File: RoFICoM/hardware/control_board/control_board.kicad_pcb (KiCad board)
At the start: 2 copper layers, 46 x 46 mm, 44 parts, among them J1 Skirt Cable, J2 M+, J3 M-, Q1 DMP6050SFG, Q2 SSM3K72KCT, Q3 DMP6050SFG, Q4 DMP6050SFG, Q5 SSM3K72KCT, Q6 DMP6050SFG, U1 STM32G071GBU6, U2 DRV8837C, U3 BU52272NUZ, U4 MIC5365, U5 BU52272NUZ, U6 ACS70331, U7 ACS70331

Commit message: RoFICoM: Route ContorlBoard v0.2
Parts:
- added C8: 470n, Capacitor_SMD:C_0402_1005Metric, F.Cu at (128.2, 74.3)
- added J4: SWD, Connector_PinHeader_2.54mm:PinHeader_1x05_P2.54mm_Vertical, F.Cu at (134.8, 79.4)
- added J5: DBG_UART, Connector_PinSocket_2.54mm:PinSocket_1x03_P2.54mm_Vertical, F.Cu at (134.8, 76.8)
- added J6: SYS_CON, rofi:pogo_row_4_3, F.Cu at (140.0, 107.0)
- added J7: SLIDER, Connector_PinHeader_1.27mm:PinHeader_1x01_P1.27mm_Vertical, F.Cu at (147.8, 79.1)
- moved R7 63.0 mm to (121.5, 100.3), turned to 270 degrees
- moved R11 62.5 mm to (121.5, 95.3), turned to 270 degrees
- moved U7 62.0 mm to (125.7, 100.3), turned to 180 degrees
- moved R10 60.3 mm to (122.0, 98.4), turned to 180 degrees
- moved R8 60.1 mm to (122.5, 100.3), turned to 90 degrees
- moved Q5 59.0 mm to (122.3, 97.3), turned to 90 degrees
- moved R9 57.1 mm to (121.5, 93.1), turned to 90 degrees
- moved D3 56.2 mm to (122.7, 93.1)
- moved Q4 55.9 mm to (125.7, 93.1), turned to 270 degrees
- moved C7 55.8 mm to (126.7, 102.6), turned to 180 degrees
- moved Q6 53.8 mm to (125.7, 96.6), turned to 270 degrees
- moved D1 38.8 mm to (153.1, 83.5)
- moved Q1 38.0 mm to (125.8, 80.5), turned to 270 degrees
- moved D2 35.9 mm to (122.9, 80.5), turned to 90 degrees
- moved R4 35.1 mm to (121.7, 80.5), turned to 90 degrees
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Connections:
- C2 pad 1: +3V3 -> GND
- C2 pad 2: GND -> +3V3
- U1 pad 1: IN_U -> INT_U
- U1 pad 11: INT_U -> LIMIT_2
- U1 pad 13: INT_I -> LIMIT_1
- U1 pad 14: EXT_U -> POT_SENSE
- U1 pad 17: SENSE_B -> SENSE_A
- U1 pad 2: Net-(U1-Pad2) -> INT_SW
- U1 pad 20: EXT_SW -> SENSE_B
- U1 pad 23: LIMIT_1 -> EXT_I
- U1 pad 24: LIMIT_2 -> EXT_U
- U1 pad 25: EXT_I -> EXT_SW
- U1 pad 28: SENSE_A -> INT_I
- U1 pad 6: INT_SW -> IN_U
- U2 pad 5: MOTOR -> MOTOR_PWM
- U2 pad 6: MOTOR_PWM -> MOTOR
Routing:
- net +3V3: track 1.19 -> 142.2 mm, vias 0 -> 11
- net INT_SW: track 0.00 -> 65.8 mm, vias 0 -> 2
- net INT_U: track 1.06 -> 60.0 mm, vias 0 -> 2
- net INT_I: track 0.00 -> 57.7 mm, vias 0 -> 2
- net SPI_MISO: track 0.00 -> 52.7 mm, vias 0 -> 1
- net EXT_SW: track 0.00 -> 47.3 mm, vias 0 -> 4
- net IN_U: track 0.00 -> 47.2 mm, vias 0 -> 2
- net SPI_SS: track 0.00 -> 45.0 mm, vias 0 -> 1
- net DBG_RX: track 0.00 -> 44.3 mm, vias 0 -> 2
- net EXT_U: track 0.00 -> 41.7 mm, vias 0 -> 4
- net DBG_TX: track 0.00 -> 41.4 mm, vias 0 -> 2
- net EXT_I: track 0.00 -> 37.9 mm, vias 0 -> 2
- net GND: track 12.3 -> 49.6 mm, vias 3 -> 14
- net SPI_SCK: track 0.00 -> 37.3 mm, vias 0 -> 1
- net LIMIT_1: track 0.00 -> 34.3 mm
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- added copper zone on B.Cu, net GND
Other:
- board size 46 x 46 mm -> 48.5 x 48.5 mm
- net class Default: via_dia 0.8 -> 0.6
- board text added: "CL SS IO"
- board text added: "Control Board v0.2 3/2019 ro.fi.muni.cz"
- board text added: "DBG"
- board text added: "GND 3V3 RST IO CLK"
- board text added: "GND RX TX"
- board text added: "RoFICoM"
- board text added: "SWD"
- board text added: "VCC GND INT EXT"

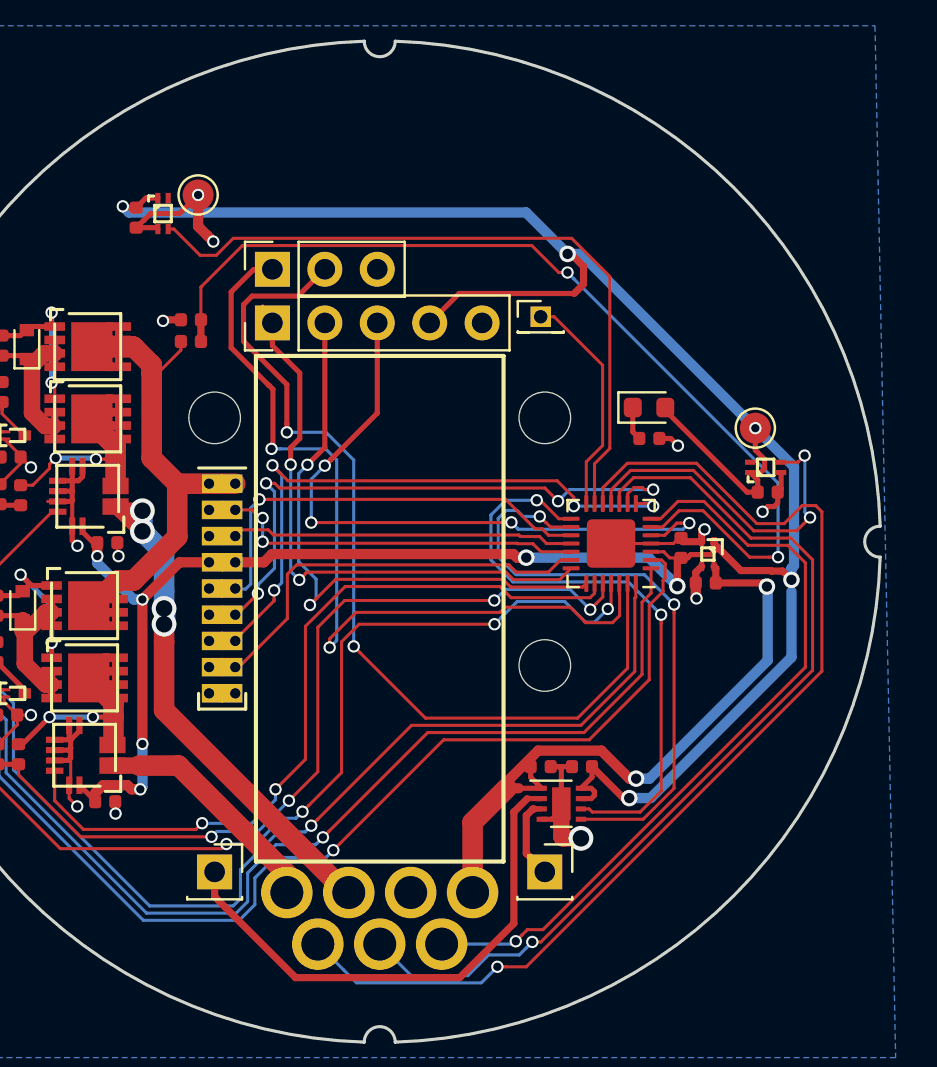
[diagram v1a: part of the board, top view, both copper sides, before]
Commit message: RoFICoM: Change footprint of the MCU
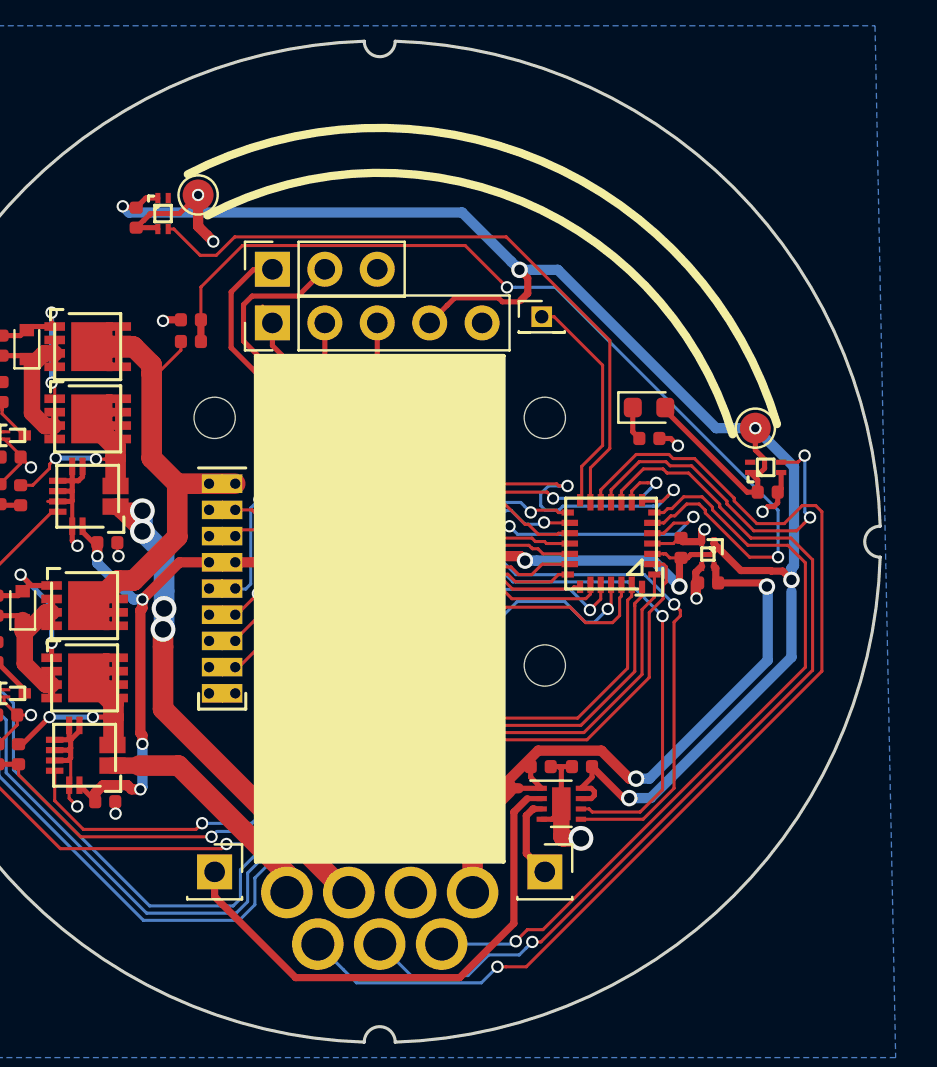
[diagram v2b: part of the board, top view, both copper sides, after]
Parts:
- U1: footprint Package_DFN_QFN:UQFN-28-1EP_4x4mm_P0.4mm_EP2.35x2.35mm -> rofi:UFQFPN28
- moved C1 0.11 mm to (155.9, 92.0)
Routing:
- net TX: track 31.3 -> 36.3 mm
- net +3V3: track 142.2 -> 138.9 mm
- net GND: track 49.6 -> 47.7 mm
- net LIMIT_1: track 34.3 -> 32.6 mm
- net RST: track 31.7 -> 32.4 mm
- net EXT_U: track 41.7 -> 41.1 mm
- net IN_U: track 47.2 -> 46.6 mm
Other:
- board text added: "Control Board v0.3 4/2019 ro.fi.muni.cz"
- board text removed: "Control Board v0.2 3/2019 ro.fi.muni.cz"

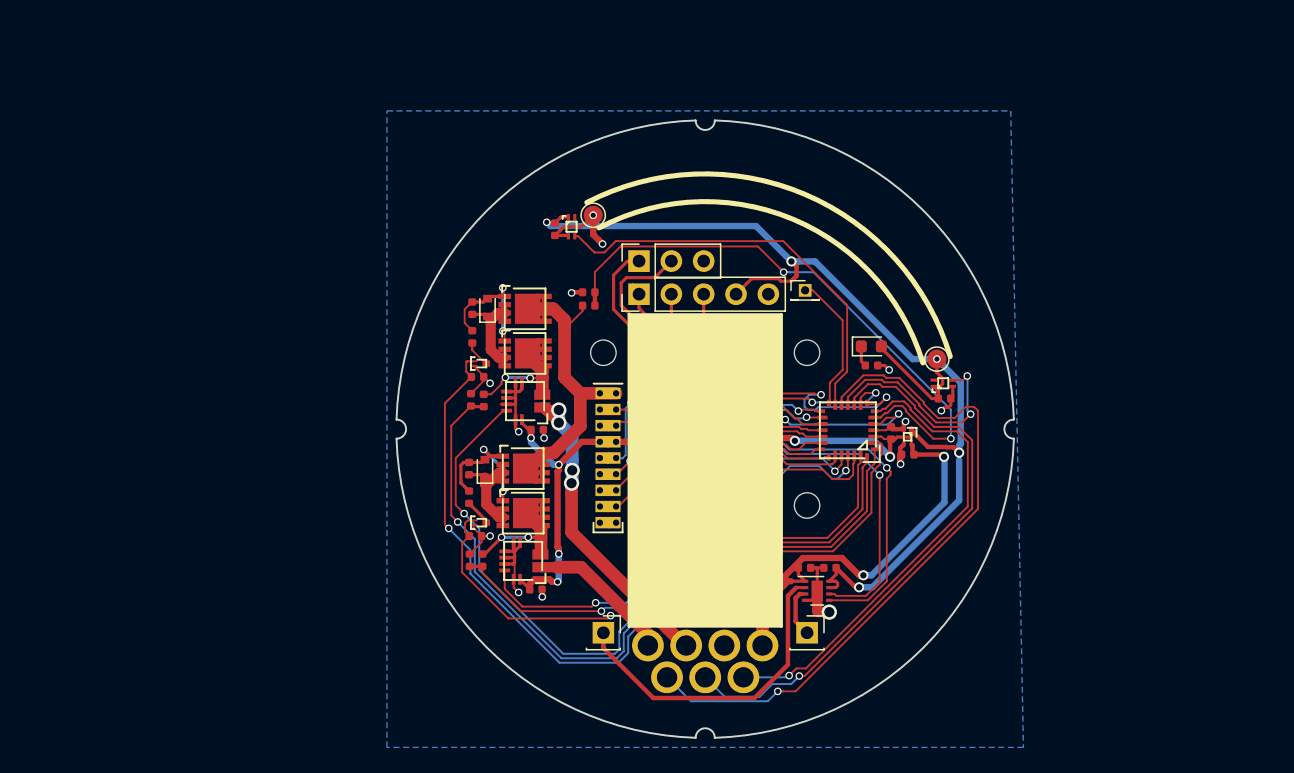
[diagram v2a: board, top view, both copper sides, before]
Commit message: RoFICoM: Add new board revision
- change voltage regulator and switching transistors
- fix wrong wiring of SWD
- add Molex board-to-board connectors for system and debugging
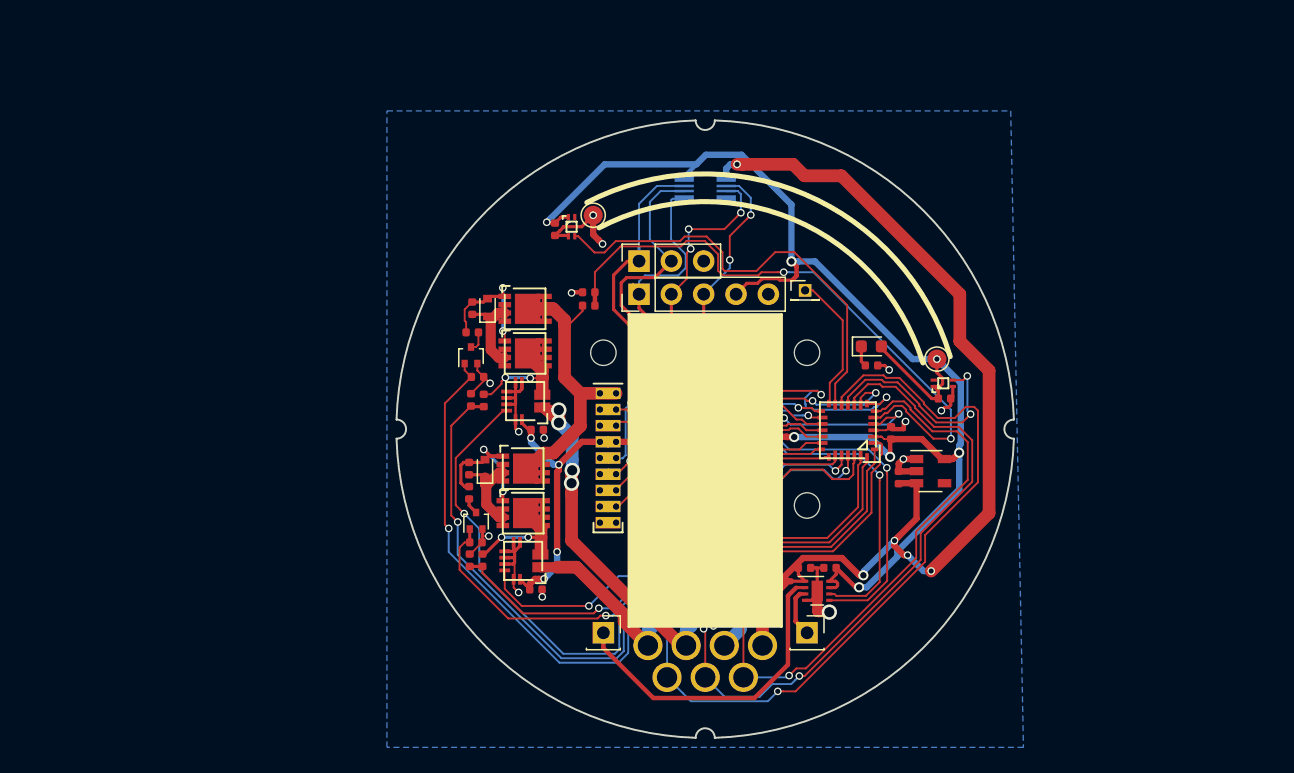
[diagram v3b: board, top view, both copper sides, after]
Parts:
- added J8: DBG, rofi:molex-505006-0812, B.Cu at (140.0, 71.1)
- added J9: SYS_CON_2, rofi:molex-505006-0812, B.Cu at (140.0, 102.5)
- Q2, Q5: value SSM3K72KCT -> SSM3K72CFS; footprint rofi:CST3 -> Package_TO_SOT_SMD:SOT-416
- U4: value MIC5365 -> NCP718ASN330T1G; footprint rofi:MLF-4 -> Package_TO_SOT_SMD:SOT-23-5
- moved U4 3.24 mm to (157.7, 93.3), turned to 0 degrees
- moved C1 1.94 mm to (155.2, 93.8), turned to 90 degrees
- moved Q2 0.96 mm to (121.6, 84.2)
- moved R10 0.50 mm to (122.0, 98.9)
- moved R11 0.35 mm to (121.5, 95.0)
- moved R6 0.35 mm to (121.7, 82.4), turned to 0 degrees
- moved Q5 0.34 mm to (122.0, 97.2)
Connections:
- U1 pad 20: SENSE_B -> SWDIO
- U1 pad 22: SWDIO -> SENSE_B
- U3 pad 4: Net-(U3-Pad4) -> (no net)
- U4 pad 1: +3V3 -> GND
- U4 pad 3: GND -> VCC
- U4 pad 4: VCC -> (no net)
- U5 pad 4: Net-(U5-Pad4) -> (no net)
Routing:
- net VCC: track 32.2 -> 84.9 mm, vias 2 -> 6
- net SPI_SCK: track 37.3 -> 50.6 mm, vias 1 -> 2
- net SWCLK: track 28.9 -> 41.2 mm
- net RST: track 32.4 -> 43.8 mm, vias 4 -> 6
- net SWDIO: track 28.6 -> 39.1 mm, vias 2 -> 5
- net DBG_TX: track 41.4 -> 51.7 mm
- net DBG_RX: track 44.4 -> 54.1 mm
- net SPI_MISO: track 53.2 -> 62.4 mm, vias 1 -> 3
- net EXT: track 11.5 -> 19.6 mm
- net +3V3: track 138.9 -> 146.6 mm
- net GND: track 47.7 -> 53.1 mm
- net SPI_SS: track 45.2 -> 50.7 mm, vias 1 -> 2
- net INT: track 25.8 -> 29.8 mm
- net LIMIT_1: track 32.6 -> 34.9 mm
- net SENSE_B: track 21.1 -> 19.6 mm
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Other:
- board text added: "Control Board v0.4 9/2019 ro.fi.muni.cz"
- board text added: "G RX TX"
- board text removed: "Control Board v0.3 4/2019 ro.fi.muni.cz"
- board text removed: "GND RX TX"

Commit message: RoFICoM: Fix bugs of v0.4 and introduce v0.5
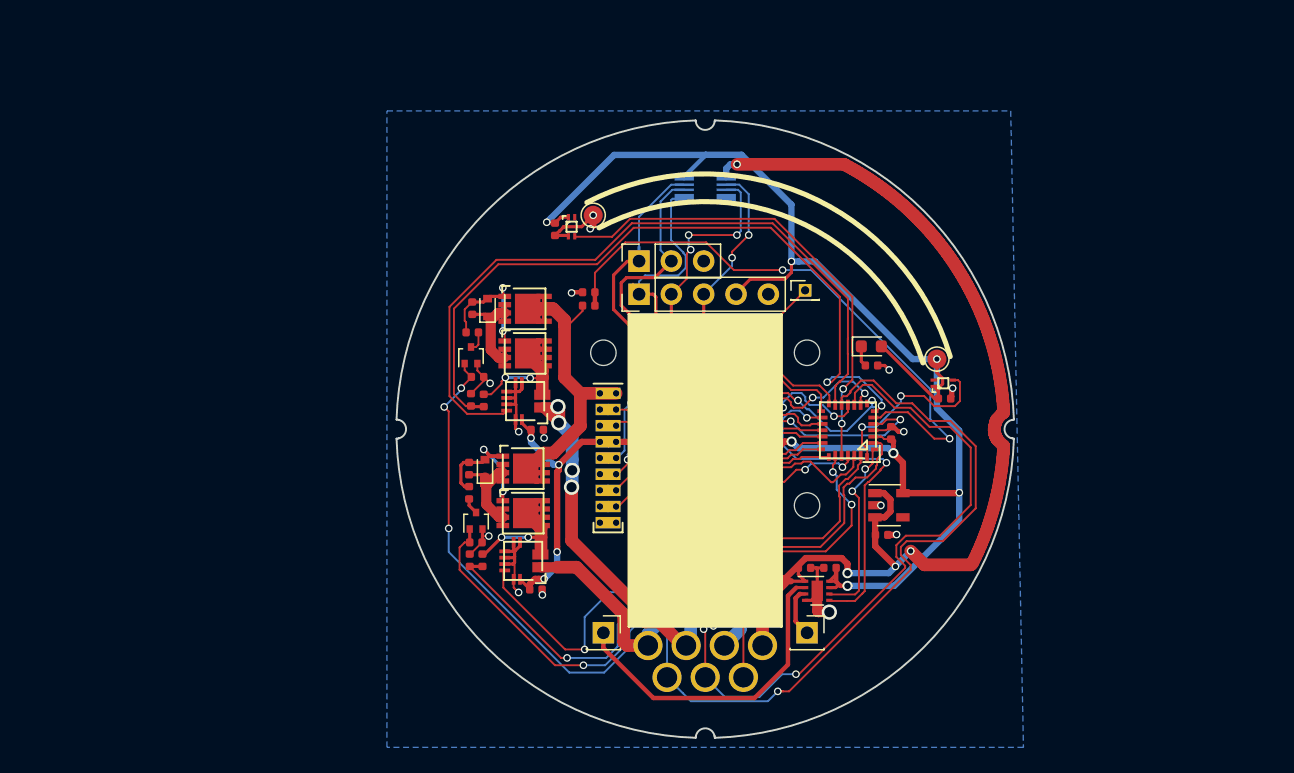
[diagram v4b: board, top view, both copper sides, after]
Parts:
- moved C1 4.70 mm to (153.9, 98.3), turned to 0 degrees
- moved U4 4.23 mm to (154.4, 96.0)
- moved J9 0.50 mm to (140.0, 102.0)
- moved J8 0.10 mm to (140.0, 71.0)
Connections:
- U1 pad 1: INT_U -> MOTOR
- U1 pad 11: LIMIT_2 -> EXT_U
- U1 pad 13: LIMIT_1 -> INT_I
- U1 pad 15: MOTOR -> EXT_I
- U1 pad 23: EXT_I -> SPI_SCK
- U1 pad 24: EXT_U -> LIMIT_1
- U1 pad 28: INT_I -> LIMIT_2
- U1 pad 7: SPI_SCK -> INT_U
- U4 pad 1: GND -> VCC
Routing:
- net SPI_SCK: track 50.6 -> 31.7 mm, vias 2 -> 3
- net EXT_I: track 36.6 -> 51.0 mm, vias 2 -> 4
- net MOTOR: track 28.9 -> 14.6 mm
- net EXT_U: track 41.6 -> 55.1 mm, vias 4 -> 6
- net GND: track 53.1 -> 48.0 mm, vias 14 -> 15
- net EXT_SW: track 48.3 -> 52.1 mm
- net LIMIT_1: track 34.9 -> 38.0 mm, vias 0 -> 2
- net TX: track 36.7 -> 33.6 mm
- net VCC: track 84.9 -> 87.8 mm, vias 6 -> 5
- net LIMIT_2: track 17.0 -> 14.1 mm
- net SWDIO: track 39.1 -> 41.8 mm
- net +3V3: track 146.6 -> 149.2 mm
- net SWCLK: track 41.2 -> 43.9 mm
- net POT_SENSE: track 10.9 -> 12.9 mm
- net INT_U: track 60.2 -> 58.4 mm
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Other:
- outline, holes or cut-outs redrawn
- rule pad_to_mask_clearance: 0.051 -> 0
- rule via_min_drill: 0.4 -> 0.3
- board text added: "Control Board v0.5 8/2020 ro.fi.muni.cz"
- board text added: "INT EXT"
- board text added: "VCC GND"
- board text removed: "Control Board v0.4 9/2019 ro.fi.muni.cz"
- board text removed: "VCC GND INT EXT"
